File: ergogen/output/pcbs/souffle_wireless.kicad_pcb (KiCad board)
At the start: 2 copper layers, 130.3 x 93.2 mm, 128 parts

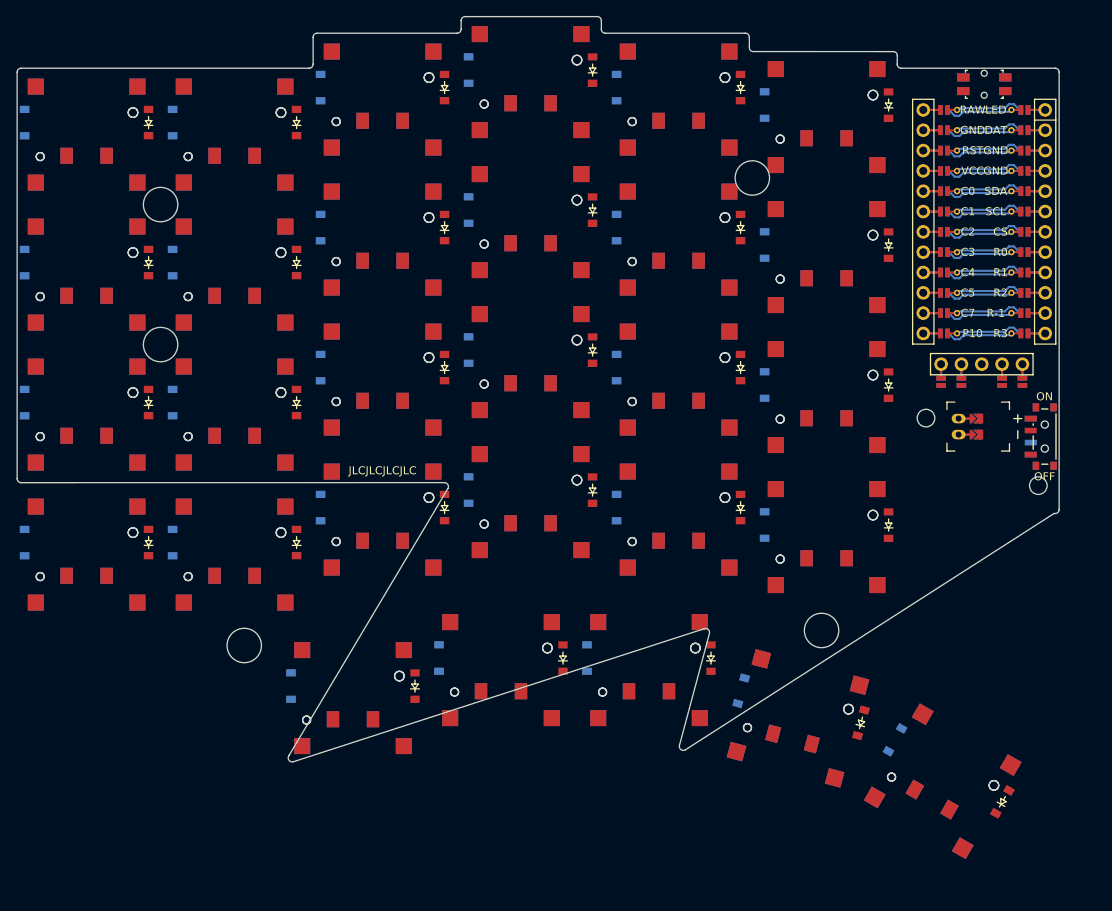
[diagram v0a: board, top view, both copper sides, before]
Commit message: fix: number row on top and improved outline
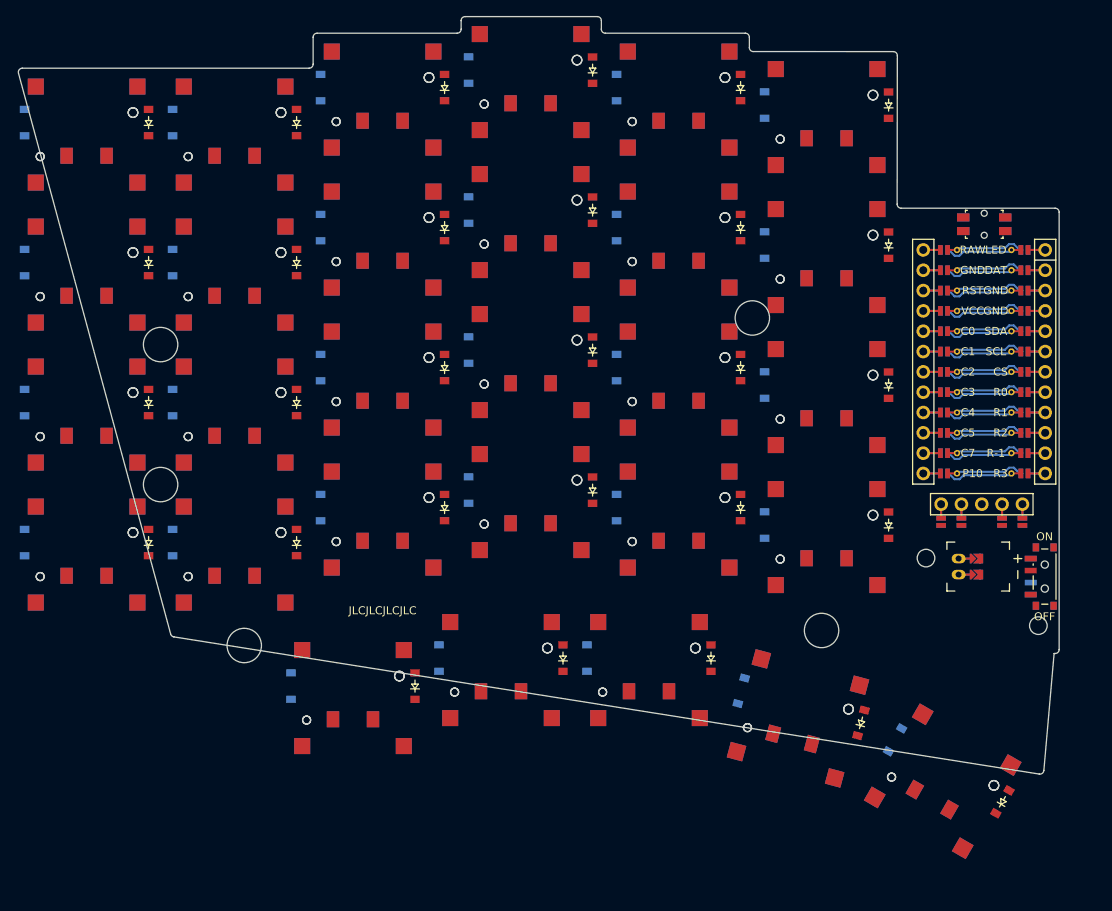
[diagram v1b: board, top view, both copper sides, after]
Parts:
- moved MCU1 17.5 mm to (212.2, 74.6)
- moved MH5 17.5 mm to (183.2, 70.4)
- moved DISP1 17.5 mm to (211.9, 77.0)
- moved JST1 17.5 mm to (209.0, 101.5)
- moved MH1 17.5 mm to (204.9, 100.4)
- moved MH2 17.5 mm to (219.0, 108.9)
- moved MH3 17.5 mm to (109.2, 73.8)
- moved MH4 17.5 mm to (109.2, 91.2)
- moved PWR1 17.5 mm to (219.8, 102.8)
- moved RST1 17.5 mm to (212.2, 58.7)
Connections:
- D1 pad 1: R-1 -> R2
- D1 pad 2: outer_number_B -> outer_bottom_B
- D10 pad 1: R2 -> R1
- D10 pad 2: ring_bottom_B -> ring_home_B
- D11 pad 1: R1 -> R0
- D11 pad 2: ring_home_B -> ring_top_B
- D12 pad 1: R0 -> R4
- D12 pad 2: ring_top_B -> ring_number_B
- D13 pad 1: R-1 -> R2
- D13 pad 2: middle_number_B -> middle_bottom_B
- D14 pad 1: R2 -> R1
- D14 pad 2: middle_bottom_B -> middle_home_B
- D15 pad 1: R1 -> R0
- D15 pad 2: middle_home_B -> middle_top_B
- D16 pad 1: R0 -> R4
- D16 pad 2: middle_top_B -> middle_number_B
- D17 pad 1: R-1 -> R2
- D17 pad 2: index_number_B -> index_bottom_B
- D18 pad 1: R2 -> R1
- D18 pad 2: index_bottom_B -> index_home_B
- D19 pad 1: R1 -> R0
- D19 pad 2: index_home_B -> index_top_B
- D2 pad 1: R2 -> R1
- D2 pad 2: outer_bottom_B -> outer_home_B
- D20 pad 1: R0 -> R4
- D20 pad 2: index_top_B -> index_number_B
- D21 pad 1: R-1 -> R2
- D21 pad 2: inner_number_B -> inner_bottom_B
- D22 pad 1: R2 -> R1
- D22 pad 2: inner_bottom_B -> inner_home_B
- D23 pad 1: R1 -> R0
- D23 pad 2: inner_home_B -> inner_top_B
- D24 pad 1: R0 -> R4
- D24 pad 2: inner_top_B -> inner_number_B
- D3 pad 1: R1 -> R0
- D3 pad 2: outer_home_B -> outer_top_B
- D30 pad 1: R-1 -> R2
- D30 pad 2: outer_number_F -> outer_bottom_F
- D31 pad 1: R2 -> R1
- D31 pad 2: outer_bottom_F -> outer_home_F
- D32 pad 1: R1 -> R0
- D32 pad 2: outer_home_F -> outer_top_F
- D33 pad 1: R0 -> R4
- D33 pad 2: outer_top_F -> outer_number_F
- D34 pad 1: R-1 -> R2
- D34 pad 2: pinky_number_F -> pinky_bottom_F
- D35 pad 1: R2 -> R1
- D35 pad 2: pinky_bottom_F -> pinky_home_F
- D36 pad 1: R1 -> R0
- D36 pad 2: pinky_home_F -> pinky_top_F
- D37 pad 1: R0 -> R4
- D37 pad 2: pinky_top_F -> pinky_number_F
- D38 pad 1: R-1 -> R2
- D38 pad 2: ring_number_F -> ring_bottom_F
- D39 pad 1: R2 -> R1
- D39 pad 2: ring_bottom_F -> ring_home_F
- D4 pad 1: R0 -> R4
- D4 pad 2: outer_top_B -> outer_number_B
- D40 pad 1: R1 -> R0
- D40 pad 2: ring_home_F -> ring_top_F
- D41 pad 1: R0 -> R4
- D41 pad 2: ring_top_F -> ring_number_F
- D42 pad 1: R-1 -> R2
- D42 pad 2: middle_number_F -> middle_bottom_F
- D43 pad 1: R2 -> R1
- D43 pad 2: middle_bottom_F -> middle_home_F
- D44 pad 1: R1 -> R0
- D44 pad 2: middle_home_F -> middle_top_F
- D45 pad 1: R0 -> R4
- D45 pad 2: middle_top_F -> middle_number_F
- D46 pad 1: R-1 -> R2
- D46 pad 2: index_number_F -> index_bottom_F
- D47 pad 1: R2 -> R1
- D47 pad 2: index_bottom_F -> index_home_F
- D48 pad 1: R1 -> R0
- D48 pad 2: index_home_F -> index_top_F
- D49 pad 1: R0 -> R4
- D49 pad 2: index_top_F -> index_number_F
- D5 pad 1: R-1 -> R2
- D5 pad 2: pinky_number_B -> pinky_bottom_B
- D50 pad 1: R-1 -> R2
- D50 pad 2: inner_number_F -> inner_bottom_F
- D51 pad 1: R2 -> R1
- D51 pad 2: inner_bottom_F -> inner_home_F
- D52 pad 1: R1 -> R0
- D52 pad 2: inner_home_F -> inner_top_F
- D53 pad 1: R0 -> R4
- D53 pad 2: inner_top_F -> inner_number_F
- D6 pad 1: R2 -> R1
- D6 pad 2: pinky_bottom_B -> pinky_home_B
- D7 pad 1: R1 -> R0
- D7 pad 2: pinky_home_B -> pinky_top_B
- D8 pad 1: R0 -> R4
- D8 pad 2: pinky_top_B -> pinky_number_B
- D9 pad 1: R-1 -> R2
- D9 pad 2: ring_number_B -> ring_bottom_B
- S1 pad 1: outer_number_B -> outer_bottom_B
- S10 pad 1: ring_bottom_B -> ring_home_B
- S11 pad 1: ring_home_B -> ring_top_B
- S12 pad 1: ring_top_B -> ring_number_B
- S13 pad 1: middle_number_B -> middle_bottom_B
- S14 pad 1: middle_bottom_B -> middle_home_B
- S15 pad 1: middle_home_B -> middle_top_B
- S16 pad 1: middle_top_B -> middle_number_B
- S17 pad 1: index_number_B -> index_bottom_B
- S18 pad 1: index_bottom_B -> index_home_B
- S19 pad 1: index_home_B -> index_top_B
- S2 pad 1: outer_bottom_B -> outer_home_B
- S20 pad 1: index_top_B -> index_number_B
- S21 pad 1: inner_number_B -> inner_bottom_B
- S22 pad 1: inner_bottom_B -> inner_home_B
- S23 pad 1: inner_home_B -> inner_top_B
- S24 pad 1: inner_top_B -> inner_number_B
- S3 pad 1: outer_home_B -> outer_top_B
- S30 pad 1: outer_number_F -> outer_bottom_F
- S31 pad 1: outer_bottom_F -> outer_home_F
- S32 pad 1: outer_home_F -> outer_top_F
- S33 pad 1: outer_top_F -> outer_number_F
- S34 pad 1: pinky_number_F -> pinky_bottom_F
- S35 pad 1: pinky_bottom_F -> pinky_home_F
- S36 pad 1: pinky_home_F -> pinky_top_F
- S37 pad 1: pinky_top_F -> pinky_number_F
- S38 pad 1: ring_number_F -> ring_bottom_F
- S39 pad 1: ring_bottom_F -> ring_home_F
- S4 pad 1: outer_top_B -> outer_number_B
- S40 pad 1: ring_home_F -> ring_top_F
- S41 pad 1: ring_top_F -> ring_number_F
- S42 pad 1: middle_number_F -> middle_bottom_F
- S43 pad 1: middle_bottom_F -> middle_home_F
- S44 pad 1: middle_home_F -> middle_top_F
- S45 pad 1: middle_top_F -> middle_number_F
- S46 pad 1: index_number_F -> index_bottom_F
- S47 pad 1: index_bottom_F -> index_home_F
- S48 pad 1: index_home_F -> index_top_F
- S49 pad 1: index_top_F -> index_number_F
- S5 pad 1: pinky_number_B -> pinky_bottom_B
- S50 pad 1: inner_number_F -> inner_bottom_F
- S51 pad 1: inner_bottom_F -> inner_home_F
- S52 pad 1: inner_home_F -> inner_top_F
- S53 pad 1: inner_top_F -> inner_number_F
- S6 pad 1: pinky_bottom_B -> pinky_home_B
- S7 pad 1: pinky_home_B -> pinky_top_B
- S8 pad 1: pinky_top_B -> pinky_number_B
- S9 pad 1: ring_number_B -> ring_bottom_B
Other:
- board size 130.3 x 93.2 mm -> 130.1 x 94.7 mm

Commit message: feat: outline improvements
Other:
- board size 130.1 x 94.7 mm -> 134.9 x 109.8 mm
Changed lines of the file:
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@@
     (segment (start 210.8 100.5) (end 209 100.5) (width 0.25) (layer "F.Cu") (net 117))
     (segment (start 210.8 100.5) (end 209 100.5) (width 0.25) (layer "B.Cu") (net 117))
-  (gr_line (start 110.50826649856596 109.92527651860325) (end 91.48622889852672 39.83343914341975) (layer Edge.Cuts) (stroke (width 0.15) (type default)))
-(gr_line (start 91.9687610950968 39.202482330781216) (end 127.8150135 39.201513513148655) (layer Edge.Cuts) (stroke (width 0.15) (type default)))
+  (gr_line (start 91.2502786953727 111.93679999635788) (end 91.31455549192064 39.702041598866344) (layer Edge.Cuts) (stroke (width 0.15) (type default)))
+(gr_line (start 91.81454179192065 39.202486498870485) (end 127.8150135 39.20151351314865) (layer Edge.Cuts) (stroke (width 0.15) (type default)))
 (gr_line (start 128.315 38.701513513148655) (end 128.315 35.3275) (layer Edge.Cuts) (stroke (width 0.15) (type default)))
 (gr_line (start 128.815 34.8275) (end 146.315 34.8275) (layer Edge.Cuts) (stroke (width 0.15) (type default)))
@@
 (gr_line (start 183.34287840000002 37.12312159204324) (end 200.8424827703032 37.12737825256575) (layer Edge.Cuts) (stroke (width 0.15) (type default)))
 (gr_line (start 201.34236077036712 37.628016802540515) (end 201.31863938512134 56.201861450012075) (layer Edge.Cuts) (stroke (width 0.15) (type default)))
-(gr_line (start 220.93800000000002 112.3635) (end 219.65752596395185 126.98539423067496) (layer Edge.Cuts) (stroke (width 0.15) (type default)))
-(gr_line (start 219.08114720800037 127.43560839237159) (end 110.91252714391037 110.28815311369672) (layer Edge.Cuts) (stroke (width 0.15) (type default)))
+(gr_line (start 221.6070711821377 104.9663415844974) (end 226.0923281969262 115.6359149762103) (layer Edge.Cuts) (stroke (width 0.15) (type default)))
+(gr_line (start 226.0654764006069 116.07782689603465) (end 211.09156059668345 142.27125340028437) (layer Edge.Cuts) (stroke (width 0.15) (type default)))
+(gr_line (start 210.44136417514045 142.47398553796899) (end 176.60167485384602 126.25365946744344) (layer Edge.Cuts) (stroke (width 0.15) (type default)))
+(gr_line (start 176.4280428580794 126.20634746780448) (end 161.62301991140092 124.94372737349019) (layer Edge.Cuts) (stroke (width 0.15) (type default)))
+(gr_line (start 161.4782637171782 124.95248967103738) (end 144.8505883399894 128.42692930209176) (layer Edge.Cuts) (stroke (width 0.15) (type default)))
+(gr_line (start 144.74831955000005 128.4375) (end 124.6650889942857 128.4375) (layer Edge.Cuts) (stroke (width 0.15) (type default)))
+(gr_line (start 124.44649265438869 128.38718392921672) (end 91.53168215547566 112.38692882557845) (layer Edge.Cuts) (stroke (width 0.15) (type default)))
 (gr_line (start 201.81863898518517 56.7025) (end 221.068 56.7025) (layer Edge.Cuts) (stroke (width 0.15) (type default)))
-(gr_line (start 221.568 57.2025) (end 221.568 111.8635) (layer Edge.Cuts) (stroke (width 0.15) (type default)))
-(gr_line (start 221.068 112.3635) (end 220.93800000000002 112.3635) (layer Edge.Cuts) (stroke (width 0.15) (type default)))
-(gr_arc (start 91.9687610950968 39.20248233078121) (mid 91.5716065950968 39.39874303078121) (end 91.48622889509679 39.83343913078121) (layer Edge.Cuts) (stroke (width 0.15) (type default)))
+(gr_line (start 221.568 57.2025) (end 221.568 104.77257712698844) (layer Edge.Cuts) (stroke (width 0.15) (type default)))
+(gr_arc (start 91.81454179192065 39.202486498863436) (mid 91.46115449192064 39.348780598863435) (end 91.31455549192064 39.70204159886344) (layer Edge.Cuts) (stroke (width 0.15) (type default)))
 (gr_arc (start 127.81501349999999 39.201513513148655) (mid 128.1685582 39.05506211314866) (end 128.315 38.701513513148655) (layer Edge.Cuts) (stroke (width 0.15) (type default)))
 (gr_arc (start 128.815 34.8275) (mid 128.4614466 34.9739466) (end 128.315 35.3275) (layer Edge.Cuts) (stroke (width 0.15) (type default)))
@@
 (gr_arc (start 201.31863938518518 56.20186150001397) (mid 201.46485988518518 56.55582760001397) (end 201.81863908518517 56.70250000001397) (layer Edge.Cuts) (stroke (width 0.15) (type default)))
 (gr_arc (start 221.568 57.2025) (mid 221.42155340000002 56.8489466) (end 221.068 56.7025) (layer Edge.Cuts) (stroke (width 0.15) (type default)))
-(gr_arc (start 221.068 112.3635) (mid 221.42155340000002 112.2170534) (end 221.568 111.8635) (layer Edge.Cuts) (stroke (width 0.15) (type default)))
-(gr_arc (start 219.08114715922605 127.43560838463978) (mid 219.46721955922604 127.33581428463978) (end 219.65752595922604 126.98539428463978) (layer Edge.Cuts) (stroke (width 0.15) (type default)))
-(gr_arc (start 110.50826649513606 109.92527650596477) (mid 110.65681719513606 110.16640490596477) (end 110.91252709513606 110.28815320596476) (layer Edge.Cuts) (stroke (width 0.15) (type default)))
+(gr_arc (start 221.568 104.77257712698844) (mid 221.57786510000003 104.87140932698844) (end 221.6070712 104.96634152698844) (layer Edge.Cuts) (stroke (width 0.15) (type default)))
+(gr_arc (start 226.0654763790639 116.07782693371927) (mid 226.1304788790639 115.86000493371927) (end 226.0923281790639 115.63591503371926) (layer Edge.Cuts) (stroke (width 0.15) (type default)))
+(gr_arc (start 210.44136417514042 142.47398553796899) (mid 210.80631727514043 142.50044073796897) (end 211.09156057514042 142.27125343796897) (layer Edge.Cuts) (stroke (width 0.15) (type default)))
+(gr_arc (start 176.60167485384602 126.25365946744346) (mid 176.51700495384603 126.22212736744345) (end 176.42804285384602 126.20634746744345) (layer Edge.Cuts) (stroke (width 0.15) (type default)))
+(gr_arc (start 161.62301990716756 124.94372737312915) (mid 161.55032240716756 124.94283237312915) (end 161.47826370716757 124.95248957312914) (layer Edge.Cuts) (stroke (width 0.15) (type default)))
+(gr_arc (start 144.74831955000005 128.4375) (mid 144.79972635000004 128.4348503) (end 144.85058835000004 128.4269294) (layer Edge.Cuts) (stroke (width 0.15) (type default)))
+(gr_arc (start 124.4464926942857 128.3871839) (mid 124.5529327942857 128.4247586) (end 124.6650889942857 128.4375) (layer Edge.Cuts) (stroke (width 0.15) (type default)))
+(gr_arc (start 91.25027869537269 111.93679999636173) (mid 91.32631019537268 112.20229379636173) (end 91.53168219537268 112.38692879636173) (layer Edge.Cuts) (stroke (width 0.15) (type default)))
 )

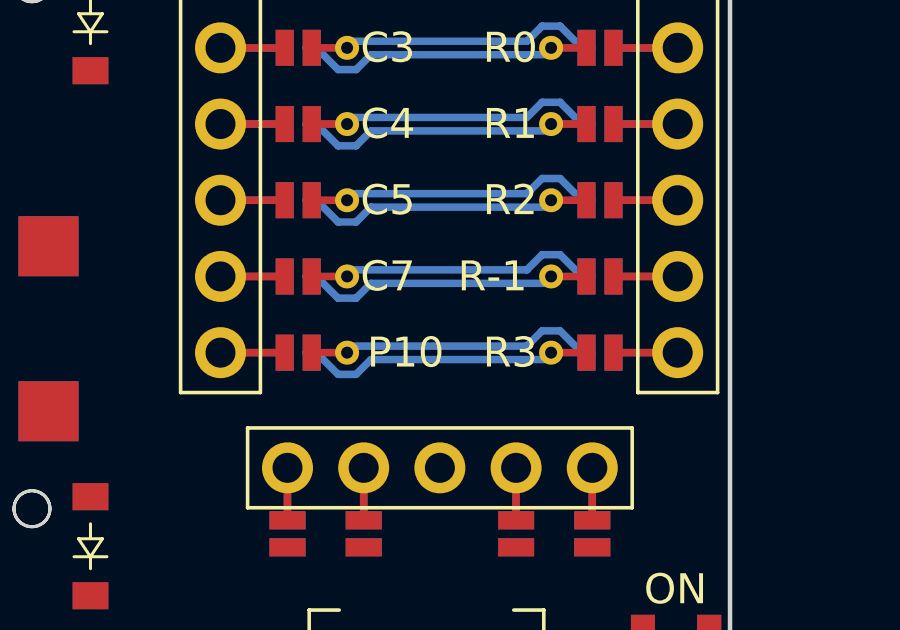
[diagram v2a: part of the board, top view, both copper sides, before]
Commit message: feat: LED and switches ratsnest
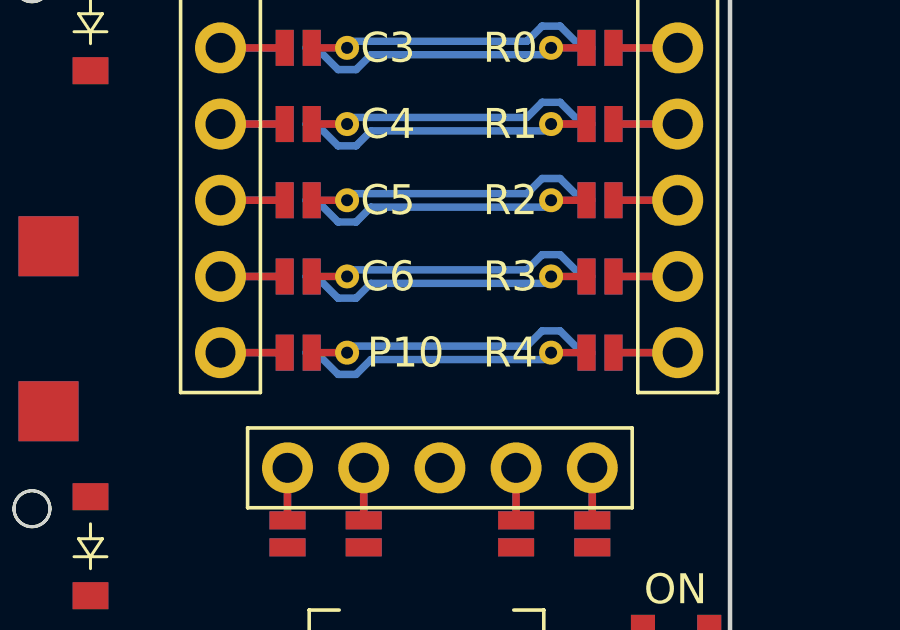
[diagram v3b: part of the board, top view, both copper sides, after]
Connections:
- D1 pad 1: R2 -> R3
- D10 pad 1: R1 -> R2
- D11 pad 1: R0 -> R1
- D12 pad 1: R4 -> R0
- D13 pad 1: R2 -> R3
- D14 pad 1: R1 -> R2
- D15 pad 1: R0 -> R1
- D16 pad 1: R4 -> R0
- D17 pad 1: R2 -> R3
- D18 pad 1: R1 -> R2
- D19 pad 1: R0 -> R1
- D2 pad 1: R1 -> R2
- D20 pad 1: R4 -> R0
- D21 pad 1: R2 -> R3
- D22 pad 1: R1 -> R2
- D23 pad 1: R0 -> R1
- D24 pad 1: R4 -> R0
- D25 pad 1: R3 -> R4
- D26 pad 1: R3 -> R4
- D27 pad 1: R3 -> R4
- D28 pad 1: R3 -> R4
- D29 pad 1: R3 -> R4
- D3 pad 1: R0 -> R1
- D30 pad 1: R2 -> R3
- D31 pad 1: R1 -> R2
- D32 pad 1: R0 -> R1
- D33 pad 1: R4 -> R0
- D34 pad 1: R2 -> R3
- D35 pad 1: R1 -> R2
- D36 pad 1: R0 -> R1
- D37 pad 1: R4 -> R0
- D38 pad 1: R2 -> R3
- D39 pad 1: R1 -> R2
- D4 pad 1: R4 -> R0
- D40 pad 1: R0 -> R1
- D41 pad 1: R4 -> R0
- D42 pad 1: R2 -> R3
- D43 pad 1: R1 -> R2
- D44 pad 1: R0 -> R1
- D45 pad 1: R4 -> R0
- D46 pad 1: R2 -> R3
- D47 pad 1: R1 -> R2
- D48 pad 1: R0 -> R1
- D49 pad 1: R4 -> R0
- D5 pad 1: R2 -> R3
- D50 pad 1: R2 -> R3
- D51 pad 1: R1 -> R2
- D52 pad 1: R0 -> R1
- D53 pad 1: R4 -> R0
- D54 pad 1: R3 -> R4
- D55 pad 1: R3 -> R4
- D56 pad 1: R3 -> R4
- D57 pad 1: R3 -> R4
- D58 pad 1: R3 -> R4
- D6 pad 1: R1 -> R2
- D7 pad 1: R0 -> R1
- D8 pad 1: R4 -> R0
- D9 pad 1: R2 -> R3
- MCU1 pad 111: R-1 -> R3
- MCU1 pad 112: R3 -> R4
- MCU1 pad 114: C7 -> C6
- S25 pad 2: C6 -> C1
- S26 pad 2: C7 -> C2
- S27 pad 2: C8 -> C3
- S28 pad 2: C9 -> C4
- S29 pad 2: C10 -> C5
- S54 pad 2: C6 -> C1
- S55 pad 2: C7 -> C2
- S56 pad 2: C8 -> C3
- S57 pad 2: C9 -> C4
- S58 pad 2: C10 -> C5

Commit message: feat: fixed pinout
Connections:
- net MCU1_12 renamed P9
- net MCU1_14 renamed P16
- D26 pad 2: middle_home_B -> mid_home_B
- D55 pad 2: middle_home_F -> mid_home_F
- MCU1 pad 10: MCU1_10 -> R2
- MCU1 pad 11: MCU1_11 -> R3
- MCU1 pad 13: MCU1_13 -> P10
- MCU1 pad 15: MCU1_15 -> C5
- MCU1 pad 16: MCU1_16 -> C4
- MCU1 pad 17: MCU1_17 -> C3
- MCU1 pad 18: MCU1_18 -> C2
- MCU1 pad 19: MCU1_19 -> C1
- MCU1 pad 20: MCU1_20 -> C0
- MCU1 pad 5: MCU1_5 -> SDA
- MCU1 pad 6: MCU1_6 -> SCL
- MCU1 pad 7: MCU1_7 -> CS
- MCU1 pad 8: MCU1_8 -> R0
- MCU1 pad 9: MCU1_9 -> R1
- S26 pad 1: middle_home_B -> mid_home_B
- S55 pad 1: middle_home_F -> mid_home_F
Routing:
- net (no net): track 333.1 -> 111.0 mm
